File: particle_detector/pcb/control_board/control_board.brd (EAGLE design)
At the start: 64 x 32 mm, 30 parts, among them IC1 LT1807R, IC3 LT3461, IC4 TEENSY 3.2

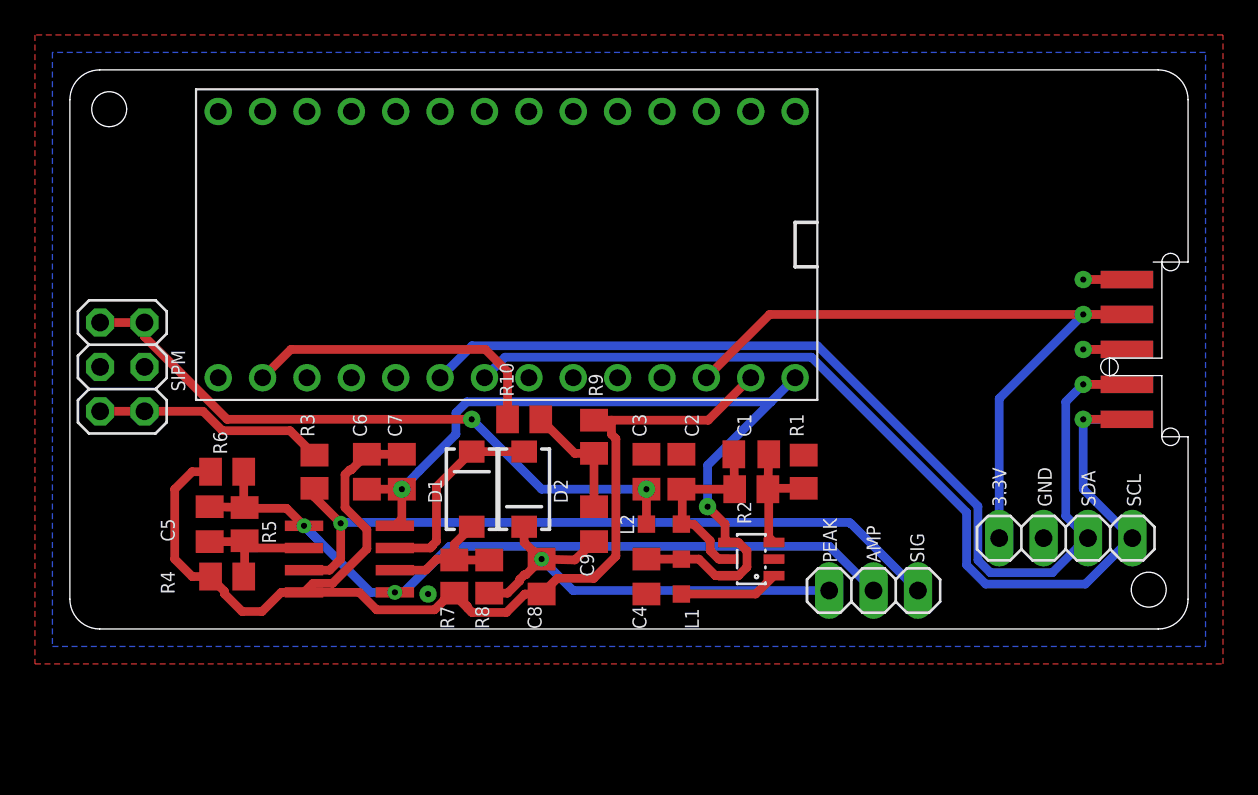
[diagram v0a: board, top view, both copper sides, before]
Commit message: move to eagle project; fix vcc/3.3v and ind package; remove full board design
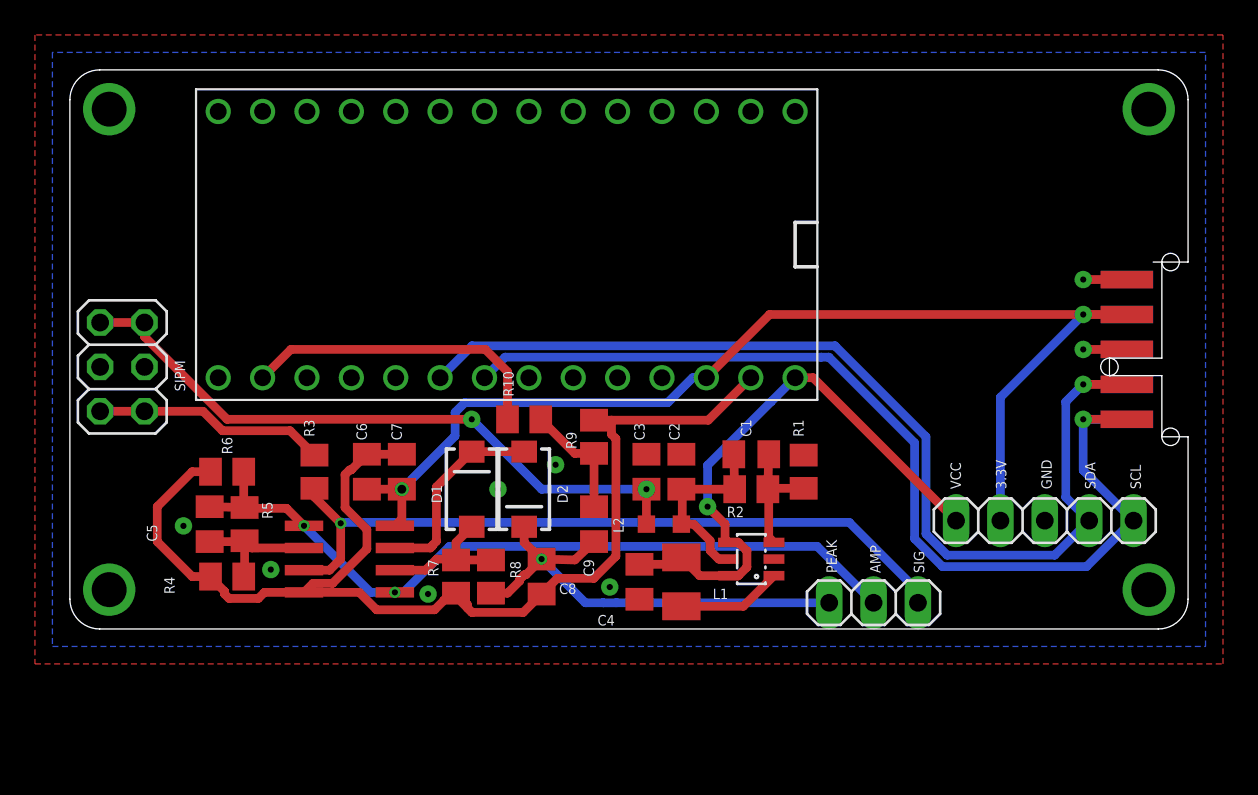
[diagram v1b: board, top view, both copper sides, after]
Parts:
- I2C: device pinhead:1X04 -> pinhead:1X05
- L1: device rcl:L2012C -> rcl:L3225M
- moved I2C 1.56 mm to (81.8, 6.20)
- moved TOUCH 0.70 mm to (72.0, 1.50)
- moved C4 0.50 mm to (58.6, 2.70)
- moved L1 0.30 mm to (61.0, 2.70)
- moved R7 0.10 mm to (48.1, 3.00)
- moved R8 0.10 mm to (50.1, 3.00)
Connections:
- net 3.3V: now also C6.1, C7.1, IC1.8
- net VCC: now also I2C.5; no longer C6.1, C7.1, IC1.8
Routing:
- net 3.3V: track 42.9 -> 67.0 mm, vias 1 -> 2
- net VCC: track 48.7 -> 33.7 mm, vias 2 -> 1
- net SIG_AMP: track 45.5 -> 44.5 mm
- net SIG_RAW: track 41.7 -> 42.4 mm
- net GND: vias 2 -> 11
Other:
- board text added: "VCC"

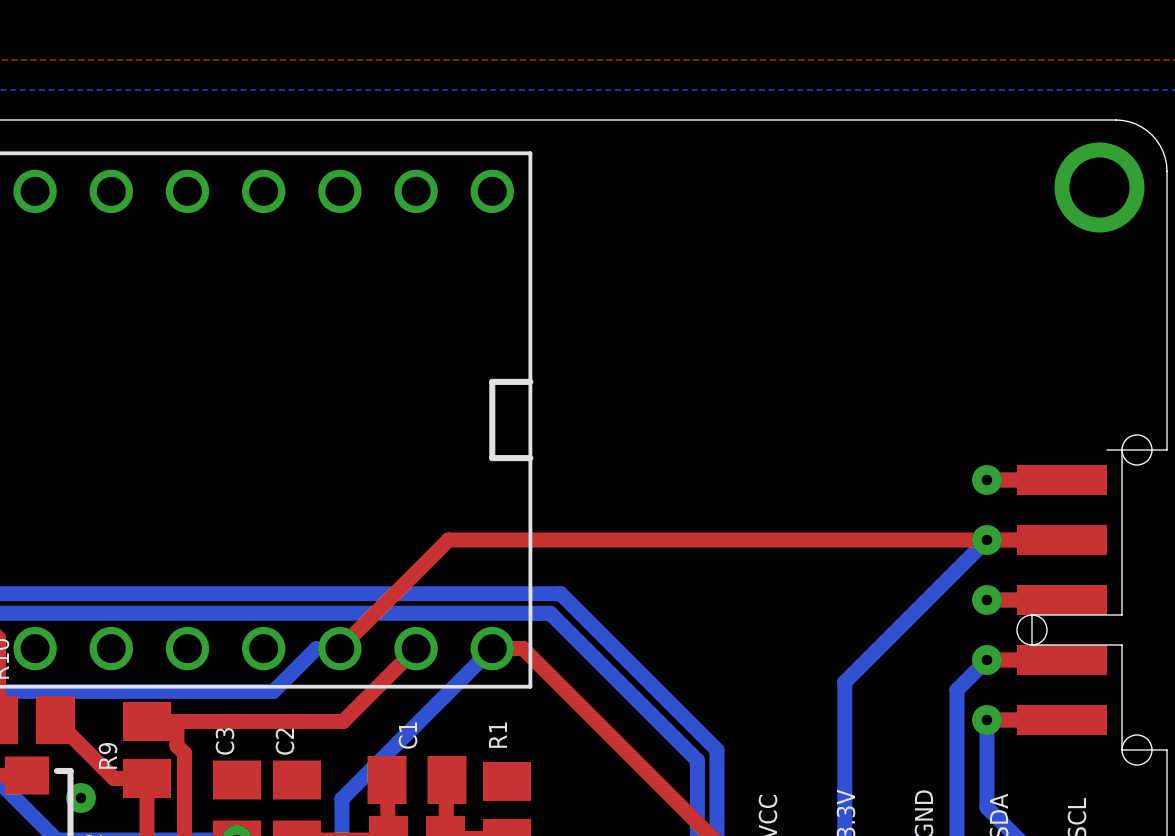
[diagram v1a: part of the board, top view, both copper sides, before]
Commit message: Stuck the TLV on there, not finished
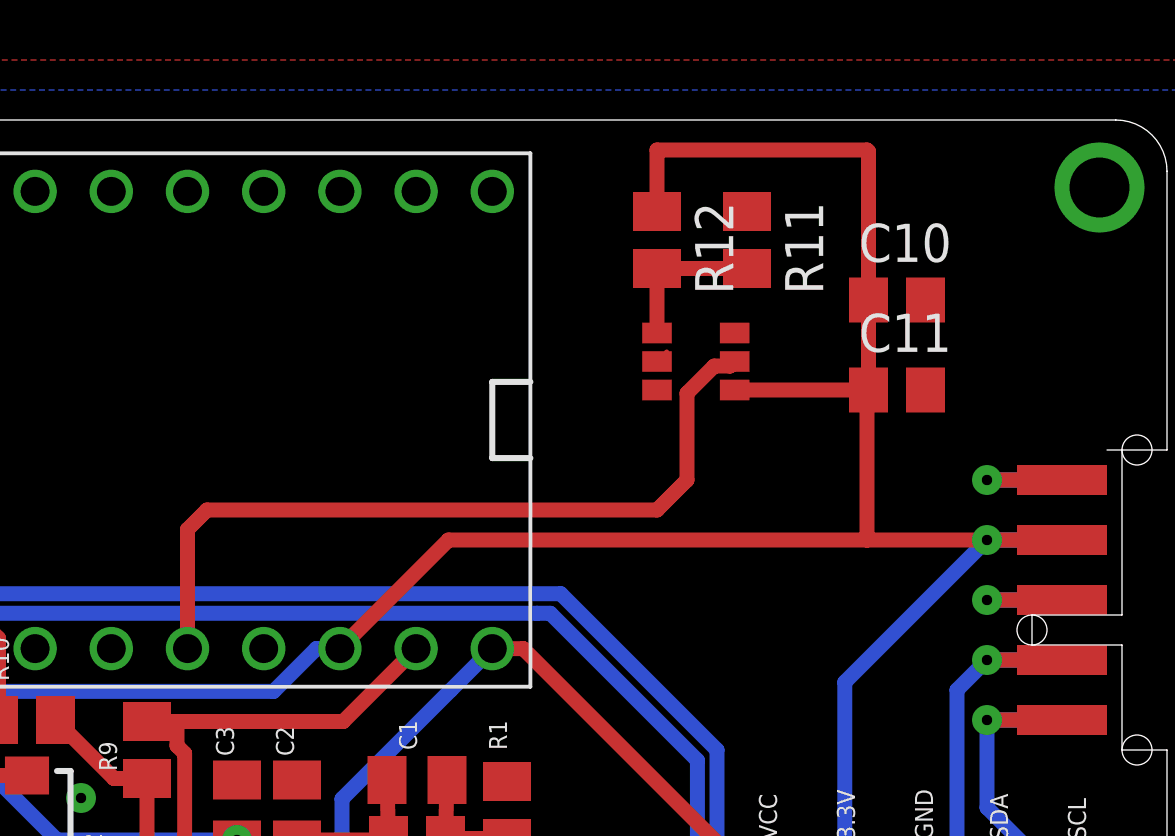
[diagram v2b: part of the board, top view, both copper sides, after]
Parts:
- added C10, C11: (no value), rcl:C0805
- added R11, R12: (no value), resistor:M0805
- added U$1: TLV3501, AU_Thinsat_Comparators:SOT23-6
- IC1: device personal:SO8 -> Personal:SO8
- IC3: device personal:SOT23-6 -> Personal:SOT23-6
- IC4: device personal:TEENSY_3.2_NO_BOTTOM -> Personal:TEENSY_3.2_NO_BOTTOM
- XBUS: device personal:XBUS_1X05_PAD -> Personal:XBUS_1X05_PAD
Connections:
- new net INT_TRIG: IC4.22/A8, U$1.P$5
- new net N$5: R11.2, R12.2, U$1.P$1
- net 3.3V: now also C10.1, C11.1, R12.1, U$1.P$4
- net GND: now also C10.2, C11.2, R11.1, U$1.P$2, U$1.P$6
- net SIG_PEAK: now also U$1.P$3
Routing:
- net 3.3V: track 67.0 -> 93.7 mm
- net INT_TRIG: track 0.00 -> 26.2 mm
- net N$5: track 0.00 -> 5.15 mm
- net GND: track 5.00 -> 5.53 mm
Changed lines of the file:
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@@
 <?xml version="1.0" encoding="utf-8"?>
 <!DOCTYPE eagle SYSTEM "eagle.dtd">
-<eagle version="9.1.1">
+<eagle version="9.1.0">
 <drawing>
 <settings>
@@
 <attribute name="PROD_ID" value="DIO-09886" x="52" y="8" size="1.778" layer="27" rot="R270" display="off"/>
 </element>
-<element name="IC1" library="personal" package="SO8" value="LT1807R" x="42" y="4" smashed="yes" rot="R270">
+<element name="IC1" library="Personal" package="SO8" value="LT1807R" x="42" y="4" smashed="yes" rot="R270">
 <attribute name="MF" value="ALTERA CORPORATION" x="42" y="4" size="1.778" layer="27" rot="R270" display="off"/>
 <attribute name="MPN" value="AD746JRZ" x="42" y="4" size="1.778" layer="27" rot="R270" display="off"/>
@@
 <attribute name="OC_NEWARK" value="59K4845" x="42" y="4" size="1.778" layer="27" rot="R270" display="off"/>
 </element>
-<element name="IC3" library="personal" package="SOT23-6" value="LT3461" x="65" y="4" smashed="yes" rot="R90"/>
-<element name="IC4" library="personal" package="TEENSY_3.2_NO_BOTTOM" value="TEENSY 3.2" x="51" y="22" smashed="yes" rot="R270">
+<element name="IC3" library="Personal" package="SOT23-6" value="LT3461" x="65" y="4" smashed="yes" rot="R90"/>
+<element name="IC4" library="Personal" package="TEENSY_3.2_NO_BOTTOM" value="TEENSY 3.2" x="51" y="22" smashed="yes" rot="R270">
 <attribute name="VALUE" x="48.19" y="22.08" size="0.6" layer="27" ratio="14"/>
 </element>
@@
 <attribute name="VALUE" x="24.555" y="18.81" size="1.27" layer="27" rot="R270"/>
 </element>
-<element name="XBUS" library="personal" package="XBUS_1X05_PAD" value="" x="86.5" y="16" smashed="yes" rot="R90">
+<element name="XBUS" library="Personal" package="XBUS_1X05_PAD" value="" x="86.5" y="16" smashed="yes" rot="R90">
 <attribute name="VALUE" x="89.675" y="11.92" size="1.27" layer="27" rot="R90"/>
 </element>
@@
 <attribute name="SPICEPREFIX" value="L" x="61" y="2.7" size="1.778" layer="27" rot="R270" display="off"/>
 <attribute name="VALUE" x="62.795" y="0.925" size="0.6" layer="27"/>
+</element>
+<element name="C10" library="rcl" library_urn="urn:adsk.eagle:library:334" package="C0805" package3d_urn="urn:adsk.eagle:package:23617/2" value="" x="81" y="26">
+<attribute name="SPICEPREFIX" value="C" x="77" y="26" size="1.778" layer="27" display="off"/>
+</element>
+<element name="R11" library="resistor" library_urn="urn:adsk.eagle:library:348" package="M0805" package3d_urn="urn:adsk.eagle:package:26079/1" value="" x="76" y="28" rot="R270"/>
+<element name="R12" library="resistor" library_urn="urn:adsk.eagle:library:348" package="M0805" package3d_urn="urn:adsk.eagle:package:26079/1" value="" x="73" y="28" rot="R270"/>
+<element name="U$1" library="AU_Thinsat_Comparators" package="SOT23-6" value="TLV3501" x="73" y="23" rot="R90"/>
+<element name="C11" library="rcl" library_urn="urn:adsk.eagle:library:334" package="C0805" package3d_urn="urn:adsk.eagle:package:23617/2" value="" x="81" y="23">
+<attribute name="SPICEPREFIX" value="C" x="81" y="23" size="1.778" layer="27" display="off"/>
 </element>
 </elements>
@@
 <via x="84" y="18" extent="1-16" drill="0.35" diameter="1"/>
 <wire x1="84" y1="18" x2="86.5" y2="18" width="0.5" layer="1"/>
-<wire x1="84" y1="18" x2="66.05" y2="18" width="0.5" layer="1"/>
+<wire x1="84" y1="18" x2="80" y2="18" width="0.5" layer="1"/>
 <contactref element="IC4" pad="3.3V"/>
+<wire x1="80" y1="18" x2="66.05" y2="18" width="0.5" layer="1"/>
 <wire x1="66.05" y1="18" x2="62.43" y2="14.38" width="0.5" layer="1"/>
 <contactref element="IC1" pad="8"/>
@@
 <wire x1="84" y1="18" x2="79.26" y2="13.26" width="0.5" layer="16"/>
 <wire x1="79.26" y1="13.26" x2="79.26" y2="6.2" width="0.5" layer="16"/>
+<contactref element="U$1" pad="P$4"/>
+<contactref element="C10" pad="1"/>
+<contactref element="C11" pad="1"/>
+<wire x1="80.05" y1="18.05" x2="80" y2="18" width="0.1524" layer="1"/>
+<wire x1="75.59" y1="23" x2="80.05" y2="23" width="0.5" layer="1"/>
+<wire x1="80.05" y1="26" x2="80.05" y2="23" width="0.5" layer="1"/>
+<wire x1="80.05" y1="23" x2="80" y2="22.95" width="0.5" layer="1"/>
+<wire x1="80" y1="22.95" x2="80" y2="18" width="0.5" layer="1"/>
+<contactref element="R12" pad="1"/>
+<wire x1="73" y1="29.04091875" x2="73" y2="28.95" width="0.5" layer="1"/>
+<wire x1="73" y1="28.95" x2="73" y2="31" width="0.5" layer="1"/>
+<wire x1="73" y1="31" x2="80" y2="31" width="0.5" layer="1"/>
+<wire x1="80" y1="31" x2="80.05" y2="30.95" width="0.5" layer="1"/>
+<wire x1="80.05" y1="30.95" x2="80.05" y2="26" width="0.5" layer="1"/>
 </signal>
 <signal name="SIGNAL">
@@
 <via x="37.5" y="3.4" extent="1-16" drill="0.35" diameter="1"/>
 <via x="32.5" y="5.9" extent="1-16" drill="0.35" diameter="1"/>
+<contactref element="U$1" pad="P$2"/>
+<contactref element="U$1" pad="P$6"/>
+<contactref element="C10" pad="2"/>
+<contactref element="C11" pad="2"/>
+<wire x1="73" y1="23.95" x2="73.3256" y2="24.2756" width="0.1524" layer="1"/>
+<wire x1="82" y1="26.05" x2="81.95" y2="26" width="0.5" layer="1"/>
+<contactref element="R11" pad="1"/>
+<wire x1="82" y1="26.05" x2="87.75" y2="29.75" width="0" layer="19" extent="1-1"/>
+<wire x1="81.95" y1="23" x2="81.95" y2="26" width="0" layer="19" extent="1-1"/>
+<wire x1="75.59" y1="24.9" x2="81.95" y2="26" width="0" layer="19" extent="1-1"/>
+<wire x1="73.3256" y1="24.2756" x2="75.59" y2="24.9" width="0" layer="19" extent="1-1"/>
+<wire x1="76" y1="28.95" x2="75.59" y2="24.9" width="0" layer="19" extent="1-1"/>
+<wire x1="84" y1="16" x2="81.95" y2="23" width="0" layer="19" extent="1-16"/>
+<wire x1="67.51" y1="29.62" x2="73" y2="23.95" width="0" layer="19" extent="1-1"/>
+<wire x1="81.8" y1="6.2" x2="84" y2="16" width="0" layer="19" extent="16-16"/>
+<wire x1="87.75" y1="2.25" x2="81.8" y2="6.2" width="0" layer="19" extent="1-1"/>
+<wire x1="68" y1="9.95" x2="81.8" y2="6.2" width="0" layer="19" extent="1-1"/>
+<wire x1="66.3" y1="4" x2="68" y2="9.95" width="0" layer="19" extent="1-1"/>
+<wire x1="61" y1="10" x2="68" y2="9.95" width="0" layer="19" extent="1-1"/>
+<wire x1="59" y1="10" x2="61" y2="10" width="0" layer="19" extent="1-1"/>
+<wire x1="53.8" y1="9.4" x2="59" y2="10" width="0" layer="19" extent="1-1"/>
+<wire x1="50.5" y1="8" x2="53.8" y2="9.4" width="0" layer="19" extent="1-1"/>
+<wire x1="46.5" y1="2" x2="50.5" y2="8" width="0" layer="19" extent="1-1"/>
+<wire x1="56.9" y1="2.4" x2="53.8" y2="9.4" width="0" layer="19" extent="1-1"/>
+<wire x1="58.6" y1="1.7" x2="56.9" y2="2.4" width="0" layer="19" extent="1-1"/>
+<wire x1="37.5" y1="3.4" x2="46.5" y2="2" width="0" layer="19" extent="1-1"/>
+<wire x1="32.5" y1="5.9" x2="37.5" y2="3.4" width="0" layer="19" extent="1-1"/>
+<wire x1="28.25" y1="2.25" x2="32.5" y2="5.9" width="0" layer="19" extent="1-1"/>
+<wire x1="30.27" y1="15" x2="32.5" y2="5.9" width="0" layer="19" extent="1-1"/>
+<wire x1="27.73" y1="15" x2="30.27" y2="15" width="0" layer="19" extent="1-1"/>
+<wire x1="28.25" y1="29.75" x2="27.73" y2="15" width="0" layer="19" extent="1-1"/>
 </signal>
 <signal name="HV">
@@
 <wire x1="57.2737875" y1="1.4976" x2="57.2761875" y2="1.5" width="0.5" layer="16"/>
 <wire x1="57.2761875" y1="1.5" x2="69.46" y2="1.5" width="0.5" layer="16"/>
+<contactref element="U$1" pad="P$3"/>
+<wire x1="73" y1="23" x2="50.1" y2="2.05" width="0" layer="19" extent="1-1"/>
 </signal>
 <signal name="N$9">
@@
 <wire x1="86.5" y1="20" x2="84" y2="20" width="0.5" layer="16"/>
 </signal>
+<signal name="N$5">
+<contactref element="U$1" pad="P$1"/>
+<contactref element="R12" pad="2"/>
+<contactref element="R11" pad="2"/>
+<wire x1="73" y1="24.9" x2="73" y2="27.05" width="0.5" layer="1"/>
+<wire x1="73" y1="27.05" x2="76" y2="27.05" width="0.5" layer="1"/>
+</signal>
+<signal name="INT_TRIG">
+<contactref element="IC4" pad="22/A8"/>
+<contactref element="U$1" pad="P$5"/>
+<wire x1="75.59" y1="23.95" x2="75.4382" y2="23.7982" width="0.5" layer="1"/>
+<wire x1="75.4382" y1="23.7982" x2="74.90728125" y2="23.7982" width="0.5" layer="1"/>
+<wire x1="74.90728125" y1="23.7982" x2="74" y2="22.89091875" width="0.5" layer="1"/>
+<wire x1="74" y1="22.89091875" x2="74" y2="20" width="0.5" layer="1"/>
+<wire x1="74" y1="20" x2="73" y2="19" width="0.5" layer="1"/>
+<wire x1="73" y1="19" x2="58" y2="19" width="0.5" layer="1"/>
+<wire x1="58" y1="19" x2="57.35" y2="18.35" width="0.5" layer="1"/>
+<wire x1="57.35" y1="18.35" x2="57.35" y2="14.38" width="0.5" layer="1"/>
+</signal>
 </signals>

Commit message: reroute traces and fix footprint for TLV chip
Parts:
- removed U$1: TLV3501, AU_Thinsat_Comparators:SOT23-6
- added IC2: TLV3501, AU_Thinsat_Comparators:SOT23-6
- C10: value (none) -> 10uF
- C11: value (none) -> 0.1uF
- IC1: device Personal:SO8 -> personal:SO8
- IC3: device Personal:SOT23-6 -> personal:SOT23-6
- IC4: device Personal:TEENSY_3.2_NO_BOTTOM -> personal:TEENSY_3.2_NO_BOTTOM
- R11: value (none) -> 1k
- R12: value (none) -> 100k
- TOUCH: device pinhead:1X03 -> pinhead:1X04
- XBUS: device Personal:XBUS_1X05_PAD -> personal:XBUS_2X05_PAD
- moved R11 2.24 mm to (74.0, 29.0), turned to 180 degrees
- moved C10 2.00 mm to (79.0, 26.0)
- moved C11 2.00 mm to (79.0, 23.0)
- moved R12 1.41 mm to (74.0, 27.0), turned to 180 degrees
- moved TOUCH 1.00 mm to (73.0, 1.50)
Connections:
- removed net INT_TRIG: IC4.22/A8, U$1.P$5
- new net SIG_INT: IC2.P$5, IC4.22/A8, TOUCH.4
- net 3.3V: now also IC2.P$4, XBUS.4; no longer U$1.P$4, XBUS.P4B, XBUS.P4T
- net AGND: now also C10.2, C11.2, IC2.P$2, IC2.P$6, R11.1
- net GND: now also XBUS.3; no longer C10.2, C11.2, R11.1, U$1.P$2, U$1.P$6, XBUS.P3B, XBUS.P3T
- net N$5: now also IC2.P$1; no longer U$1.P$1
- net SCL: now also XBUS.1; no longer XBUS.P1B, XBUS.P1T
- net SDA: now also XBUS.2; no longer XBUS.P2B, XBUS.P2T
- net SIG_PEAK: now also IC2.P$3; no longer U$1.P$3
- net VBAT: now also XBUS.5; no longer XBUS.P5B, XBUS.P5T
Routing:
- net AGND: track 69.0 -> 118.9 mm
- net SIG_INT: track 0.00 -> 47.5 mm
- net INT_TRIG: track 26.2 -> 0.00 mm
- net SIG_PEAK: track 27.0 -> 51.8 mm, vias 1 -> 3
- net 3.3V: track 93.7 -> 78.8 mm
- net GND: track 5.53 -> 2.50 mm
- net VBAT: track 5.00 -> 2.50 mm
- net SCL: track 58.9 -> 56.4 mm
- net SDA: track 60.7 -> 58.2 mm
- net SIG_AMP: track 44.5 -> 46.9 mm
- net SIG_RAW: track 42.4 -> 44.3 mm
- net VCC: vias 1 -> 2
